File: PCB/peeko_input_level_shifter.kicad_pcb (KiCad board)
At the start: 2 copper layers, 18.3 x 43.2 mm, 21 parts, among them J1 Conn_02x15_Odd_Even, J2 Conn_02x15_Odd_Even, U1 TXU0104, U2 TXU0104, U3 TXU0104, U4 TXU0104, U5 TXU0104, U6 TXU0104

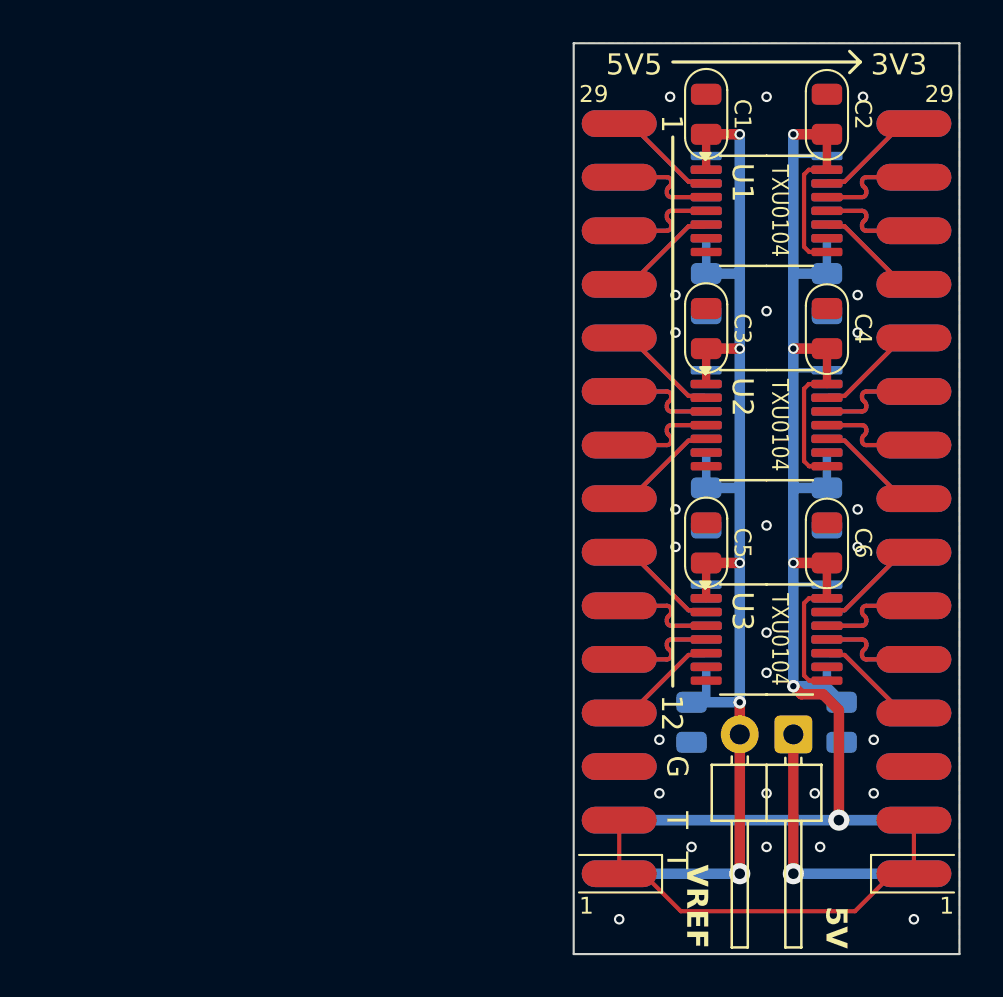
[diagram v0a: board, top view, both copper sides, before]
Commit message: local tssop14 footprint, redo short side traces on peeko+ & level shifter
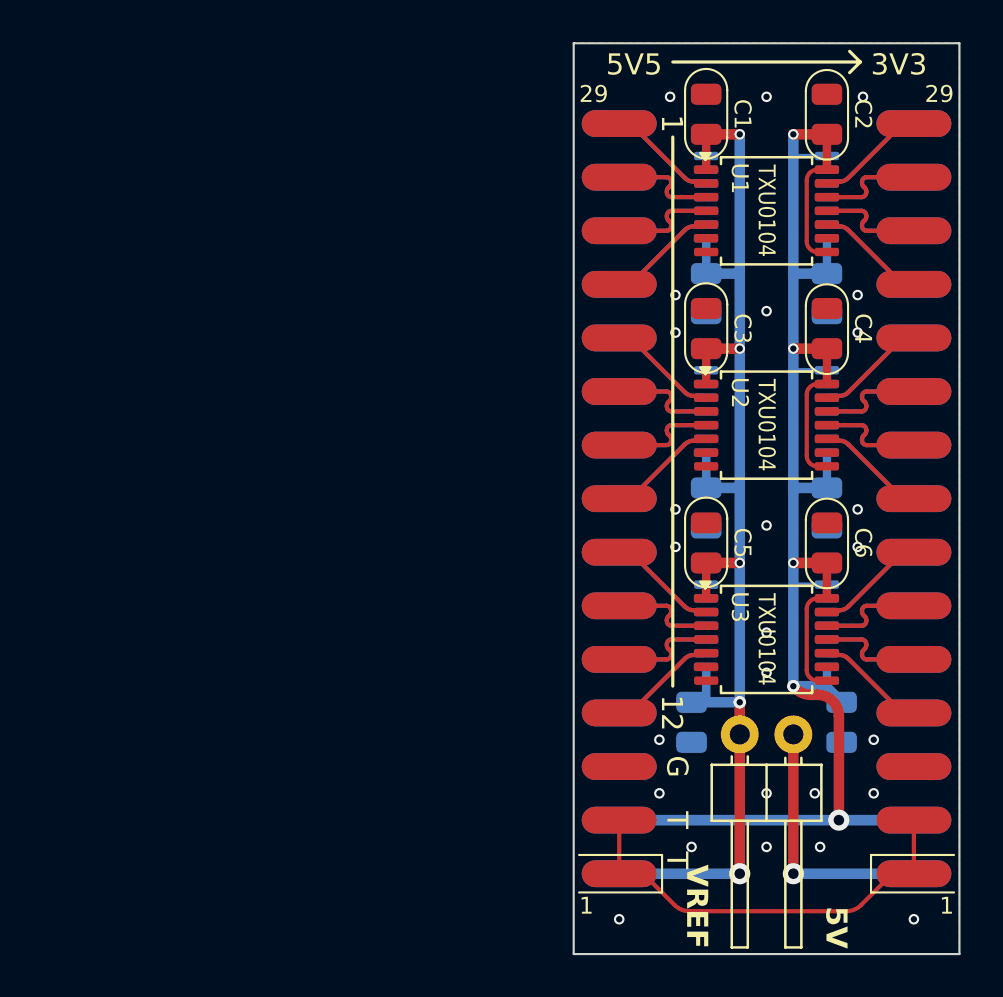
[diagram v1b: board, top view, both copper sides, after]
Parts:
- JP1: footprint 000_LOCAL:PinHeader_1x02_P2.54mm_Horizontal -> 000_LOCAL:PinHeader_1x02_P2.54mm_Horizontal jumper closed
- U1, U2, U3, U4, U5, U6: footprint Package_SO:TSSOP-14_4.4x5mm_P0.65mm -> 000_LOCAL:TSSOP-14_4.4x5mm_P0.65mm
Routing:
- net +3V3: track 91.0 -> 89.6 mm

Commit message: pics
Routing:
- net VREF: track 60.4 -> 61.8 mm, vias 5 -> 4
- net +3V3: track 89.6 -> 88.6 mm
- net GND: vias 26 -> 27

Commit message: level shifter housing
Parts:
- moved C2 38.5 mm to (129.0, 96.4), turned to 180 degrees
- moved C1 37.1 mm to (129.0, 102.1), turned to 0 degrees
- moved U6 32.2 mm to (132.9, 99.2), turned to 90 degrees
- moved U1 31.3 mm to (133.6, 99.2), turned to 90 degrees
- moved C12 27.2 mm to (137.5, 96.4), turned to 0 degrees
- moved C11 25.1 mm to (137.5, 102.1), turned to 180 degrees
- moved C4 25.1 mm to (139.1, 96.4), turned to 180 degrees
- moved C3 22.8 mm to (139.1, 102.1), turned to 0 degrees
- moved J2 22.6 mm to (147.2, 90.1), turned to -90 degrees
- moved U5 18.4 mm to (143.1, 99.2), turned to 90 degrees
- moved U2 17.5 mm to (143.7, 99.2), turned to 90 degrees
- moved C10 15.1 mm to (147.6, 96.4), turned to 0 degrees
- moved C6 13.6 mm to (149.3, 96.4), turned to 180 degrees
- moved J1 12.8 mm to (147.2, 108.4), turned to -90 degrees
- moved C8 12.4 mm to (157.8, 95.7), turned to 0 degrees
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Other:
- board size 18.3 x 43.2 mm -> 43.2 x 18.3 mm
